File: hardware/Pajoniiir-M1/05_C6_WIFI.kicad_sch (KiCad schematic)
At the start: 22 parts, among them U4 ESP32-C6-WROOM-1-N4

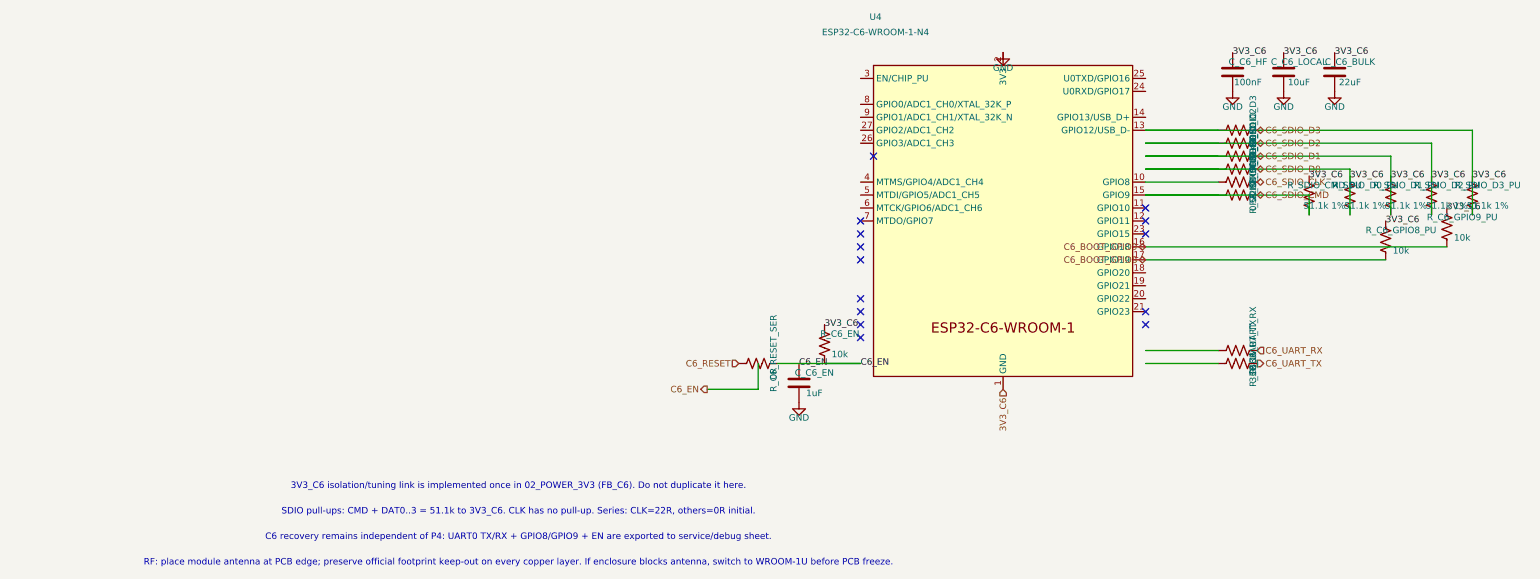
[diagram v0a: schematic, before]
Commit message: hardware: snap child sheets 01-05 to 25 mil grid
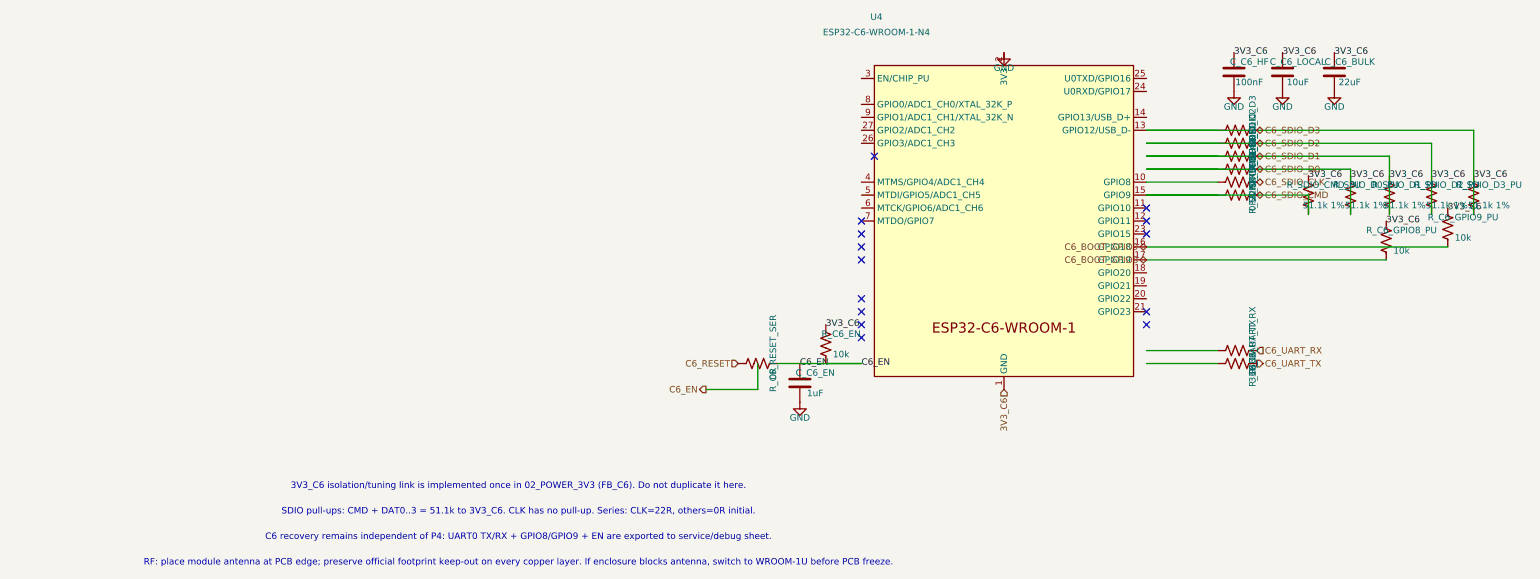
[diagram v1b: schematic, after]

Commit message: hardware: make KiCad symbol libraries reproducible
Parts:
- U4: symbol PCM_Espressif:ESP32-C6-WROOM-1 -> Pajoniiir-M1:ESP32-C6-WROOM-1
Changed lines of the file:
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@@
   )
   (symbol
-    (lib_id "PCM_Espressif:ESP32-C6-WROOM-1")
+    (lib_id "Pajoniiir-M1:ESP32-C6-WROOM-1")
     (at 130.175 80.01 0)
     (unit 1)
